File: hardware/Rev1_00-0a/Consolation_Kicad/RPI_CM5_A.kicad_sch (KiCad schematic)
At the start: 49 parts, among them J19 RPI_CMx_A, J7 2998TR, Q12 2N7002, U19 SN74LVC1G125DBVR, U21 MCP7940NT-I/MS, Y2 32.768kHz

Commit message: Update block diagram Updage charger schematic page with BQ25640 preliminary implementation
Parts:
- removed R111, R124: 4K7, footprint:RES_0402, symbol KicadCompDb:Resistors/RES_SMT_00010
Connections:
- net I2C6.I2C_SCL: no longer names the net of J19.47 (GPIO23)
- net I2C6.I2C_SDA: no longer names the net of J19.46 (GPIO22)

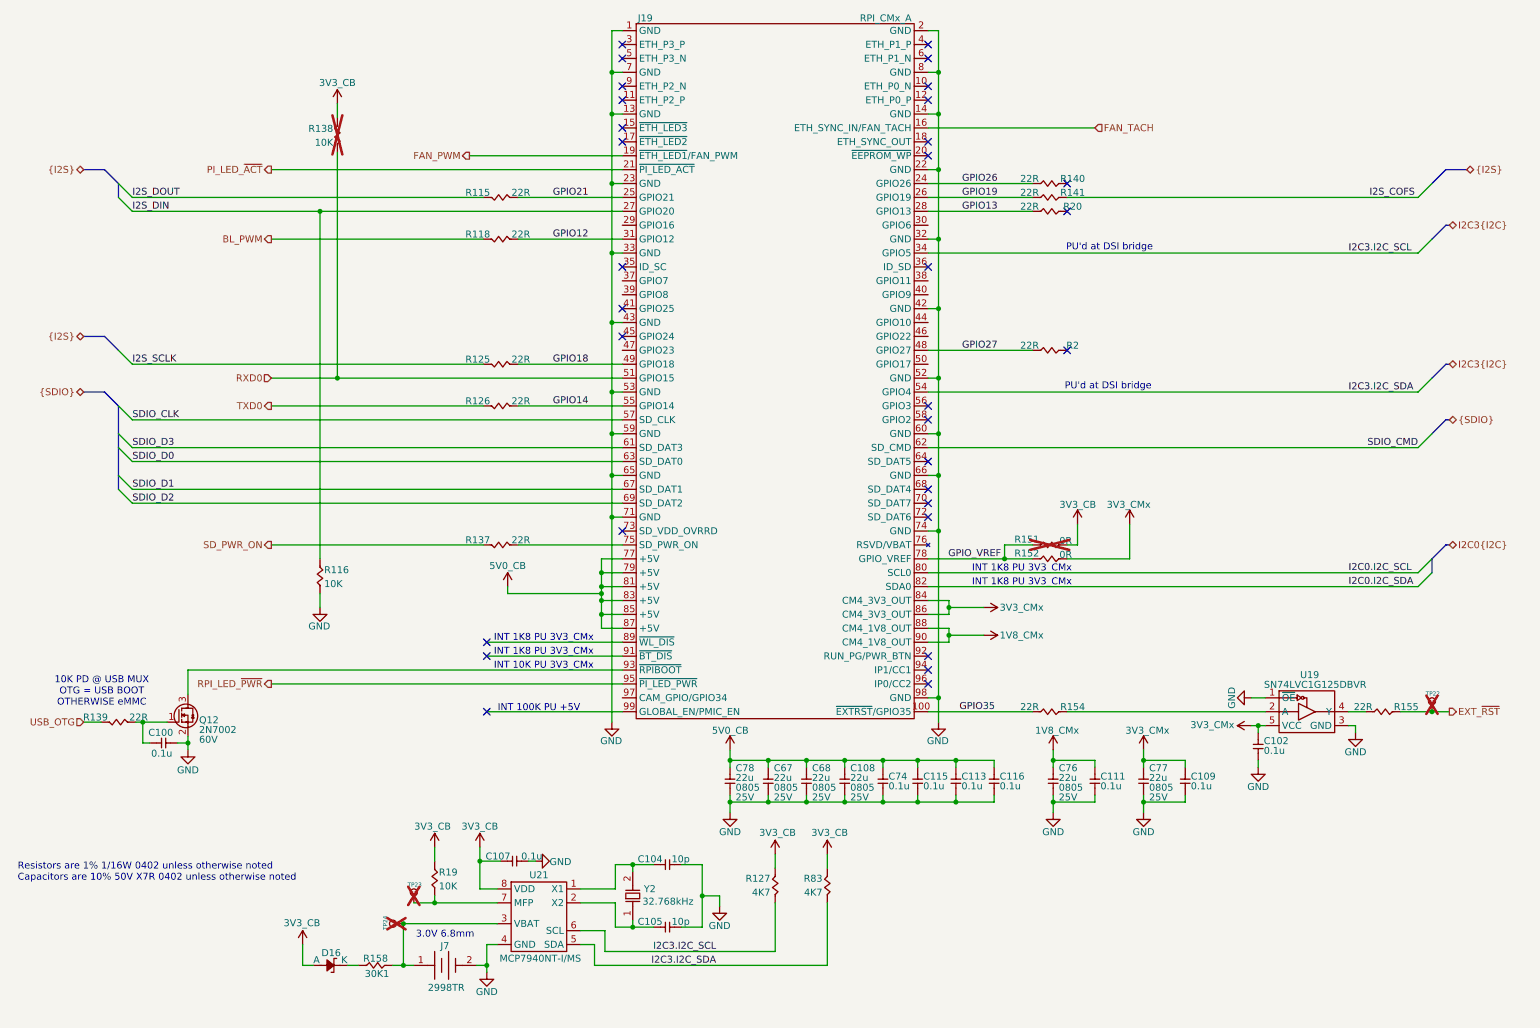
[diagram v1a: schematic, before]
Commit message: Add part number of codec to block diagram Add codec and hdmi schematic sheets
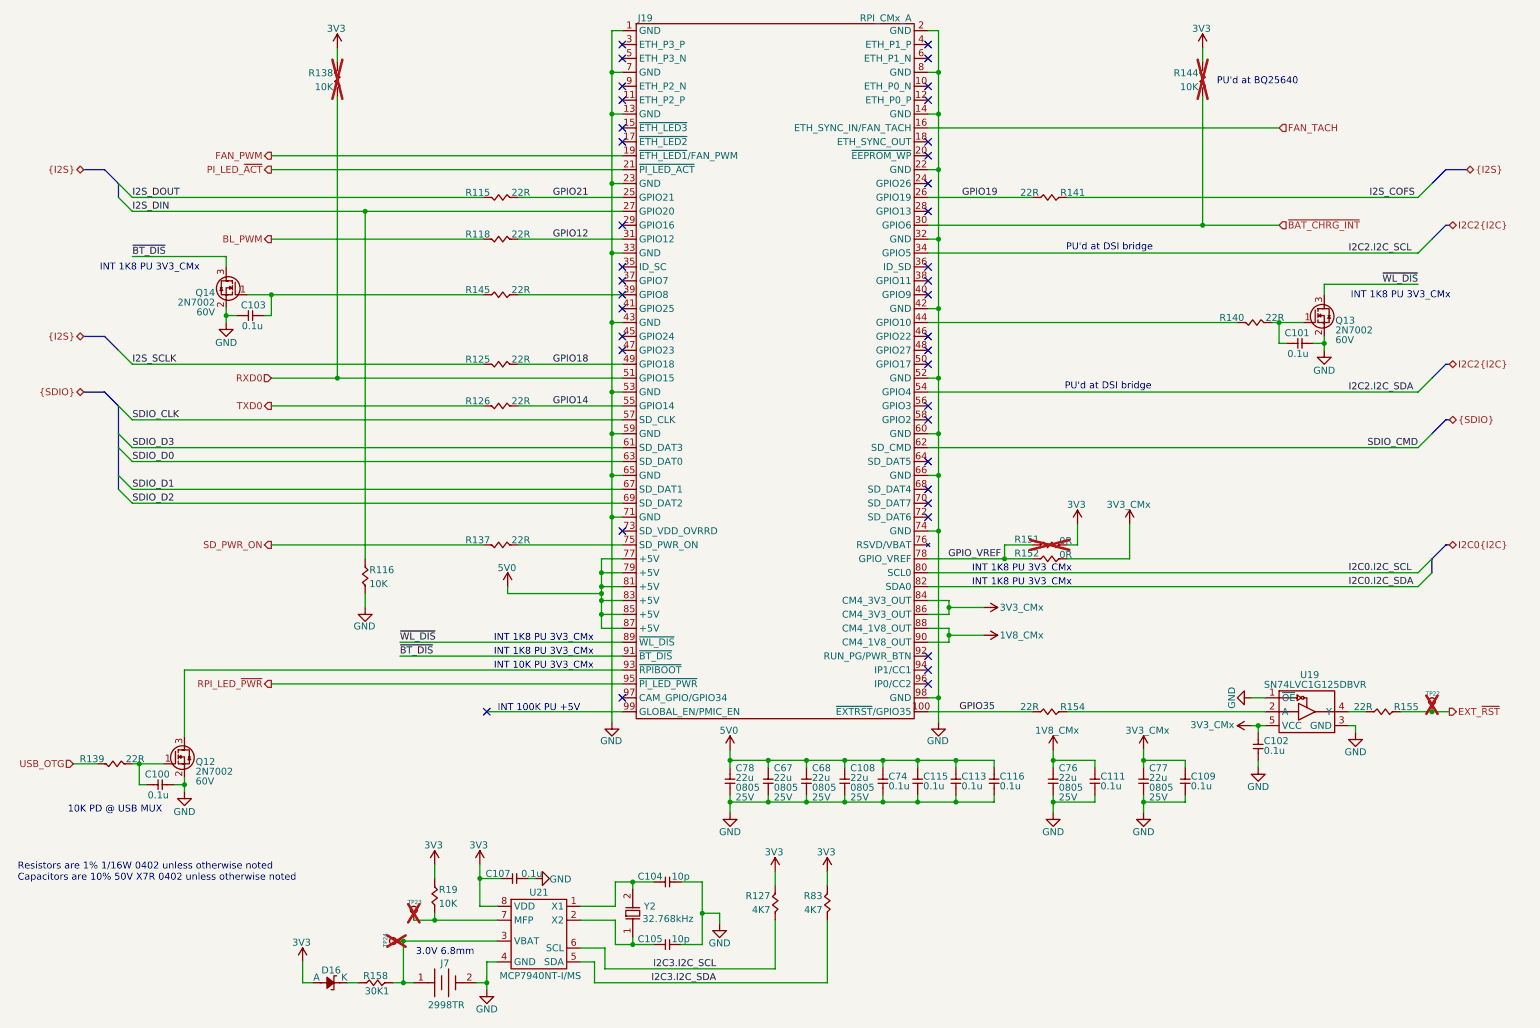
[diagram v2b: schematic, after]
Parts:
- removed R2, R20: 22R, footprint:RES_0402, symbol KicadCompDb:Resistors/RES_SMT_00015
- added C101, C103: 0.1u, footprint:CAP_NONPOL_0402, symbol KicadCompDb:Capacitors/CAP_CER_SMT_00001
- added Q13, Q14: 2N7002, footprint:SOT-23-3, symbol KicadCompDb:Mosfet/MOSFET_00001
- added R144: 10K, footprint:RES_0402, symbol KicadCompDb:Resistors/RES_SMT_00013
- added R145: 22R, footprint:RES_0402, symbol KicadCompDb:Resistors/RES_SMT_00015
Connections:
- net GND: now also C101.1, C103.1, Q13.2 (S), Q14.2 (S)
- net I2C3.I2C_SCL: no longer J19.34 (GPIO5)
- net I2C3.I2C_SDA: no longer J19.54 (GPIO4)
- net ~{BAT_CHRG_INT}: now reaches J19.30 (GPIO6)
- net ~{BAT_CHRG_INT}: now also R144.1
- net at J19.39 (GPIO8): now also R145.2
- net at J19.44 (GPIO10): now also R140.2
- net ~{WL_DIS}: now reaches J19.89 (~{WL_DIS})
- net ~{WL_DIS}: now also Q13.3 (D)
- net ~{BT_DIS}: now reaches J19.91 (~{BT_DIS})
- net ~{BT_DIS}: now also Q14.3 (D)
- net 3V3_CB renamed 3V3
- net 3V3: now also R144.2
- net 5V0_CB renamed 5V0
- net GPIO13: no longer names the net of J19.28 (GPIO13)
- net GPIO26: no longer names the net of R140.1
- net GPIO26: now also C101.2, Q13.1 (G); no longer J19.24 (GPIO26)
- net GPIO27: no longer names the net of J19.48 (GPIO27)
- new net: C103.2, Q14.1 (G), R145.1
- new net I2C2.I2C_SCL: J19.34 (GPIO5)
- new net I2C2.I2C_SDA: J19.54 (GPIO4)
- no-connect marks 32 -> 39
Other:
- note added: "10K PD @ USB MUX"
- note added: "PU'd at BQ25640"
- note removed: "10K PD @ USB MUX OTG = USB BOOT OTHERWISE eMMC"
- moved on the sheet: C100, C104, C105, C107, D16, J7, Q12, R116, R127, R138, R139, R158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

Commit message: Update schematics, block diagram and pin mux (good progress G)
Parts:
- removed TP23, TP24: 28 mils, footprint:SMT_TP_28_MILS, symbol KicadCompDb:Test Point/TP_00001
- added R117: 22R, footprint:RES_0402, symbol KicadCompDb:Resistors/RES_SMT_00015
- added R143, R156: 10K, footprint:RES_0402, symbol KicadCompDb:Resistors/RES_SMT_00013
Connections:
- net 3V3: now also R143.2, R156.2
- net FAN_PWM: now also R117.2; no longer J19.19 (~{ETH_LED1}/FAN_PWM)
- net GPIO10: now reaches J19.44 (GPIO10), R140.2
- net ~{VOL_UP}: now reaches J19.28 (GPIO13)
- net ~{VOL_UP}: now also R156.1
- net ~{VOL_DOWN}: now reaches J19.29 (GPIO16)
- net ~{VOL_DOWN}: now also R143.1
- net GPIO8: now reaches J19.39 (GPIO8), R145.2
- net PPS_RTC: now reaches J19.40 (GPIO9)
- net PPS_RTC: now also R19.1, U21.7 (MFP)
- net ~{HP_DETECT}: now reaches J19.50 (GPIO17)
- net I2C0.I2C_SCL: no longer names the net of J19.80 (SCL0)
- net I2C0.I2C_SDA: no longer names the net of J19.82 (SDA0)
- new net: J19.19 (~{ETH_LED1}/FAN_PWM), R117.1
- no-connect marks 39 -> 35
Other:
- note added: "INT 10K PU +5V"
- moved on the sheet: C100, C108, C109, C111, C113, C115, C116, C67, C68, C74, C76, C77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

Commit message: Update PinMux & Schematics
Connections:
- net RXD0 renamed CM5_RXD0
- net TXD0 renamed CM5_TXD0
- net ~{HP_DETECT}: no longer names the net of J19.50 (GPIO17)
- no-connect marks 35 -> 36
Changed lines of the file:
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@@
 	)
 	(no_connect
+		(at 179.07 78.105)
+	)
+	(no_connect
 		(at 179.07 62.865)
 	)
@@
 	(wire
 		(pts
-			(xy 179.07 78.105) (xy 227.965 78.105)
-		)
-		(stroke
-			(width 0)
-			(type default)
-		)
-	)
-	(wire
-		(pts
 			(xy 120.015 184.785) (xy 115.57 184.785)
 		)
@@
 		)
 	)
-	(hierarchical_label "RXD0"
+	(hierarchical_label "CM5_RXD0"
 		(shape input)
 		(at 74.295 80.645 180)
@@
 		)
 	)
-	(hierarchical_label "~{HP_DETECT}"
-		(shape input)
-		(at 227.965 78.105 0)
-		(effects
-			(font
-				(size 1.27 1.27)
-			)
-			(justify left)
-		)
-	)
 	(hierarchical_label "~{VOL_DOWN}"
 		(shape input)
@@
 		)
 	)
-	(hierarchical_label "TXD0"
+	(hierarchical_label "CM5_TXD0"
 		(shape output)
 		(at 74.295 85.725 180)

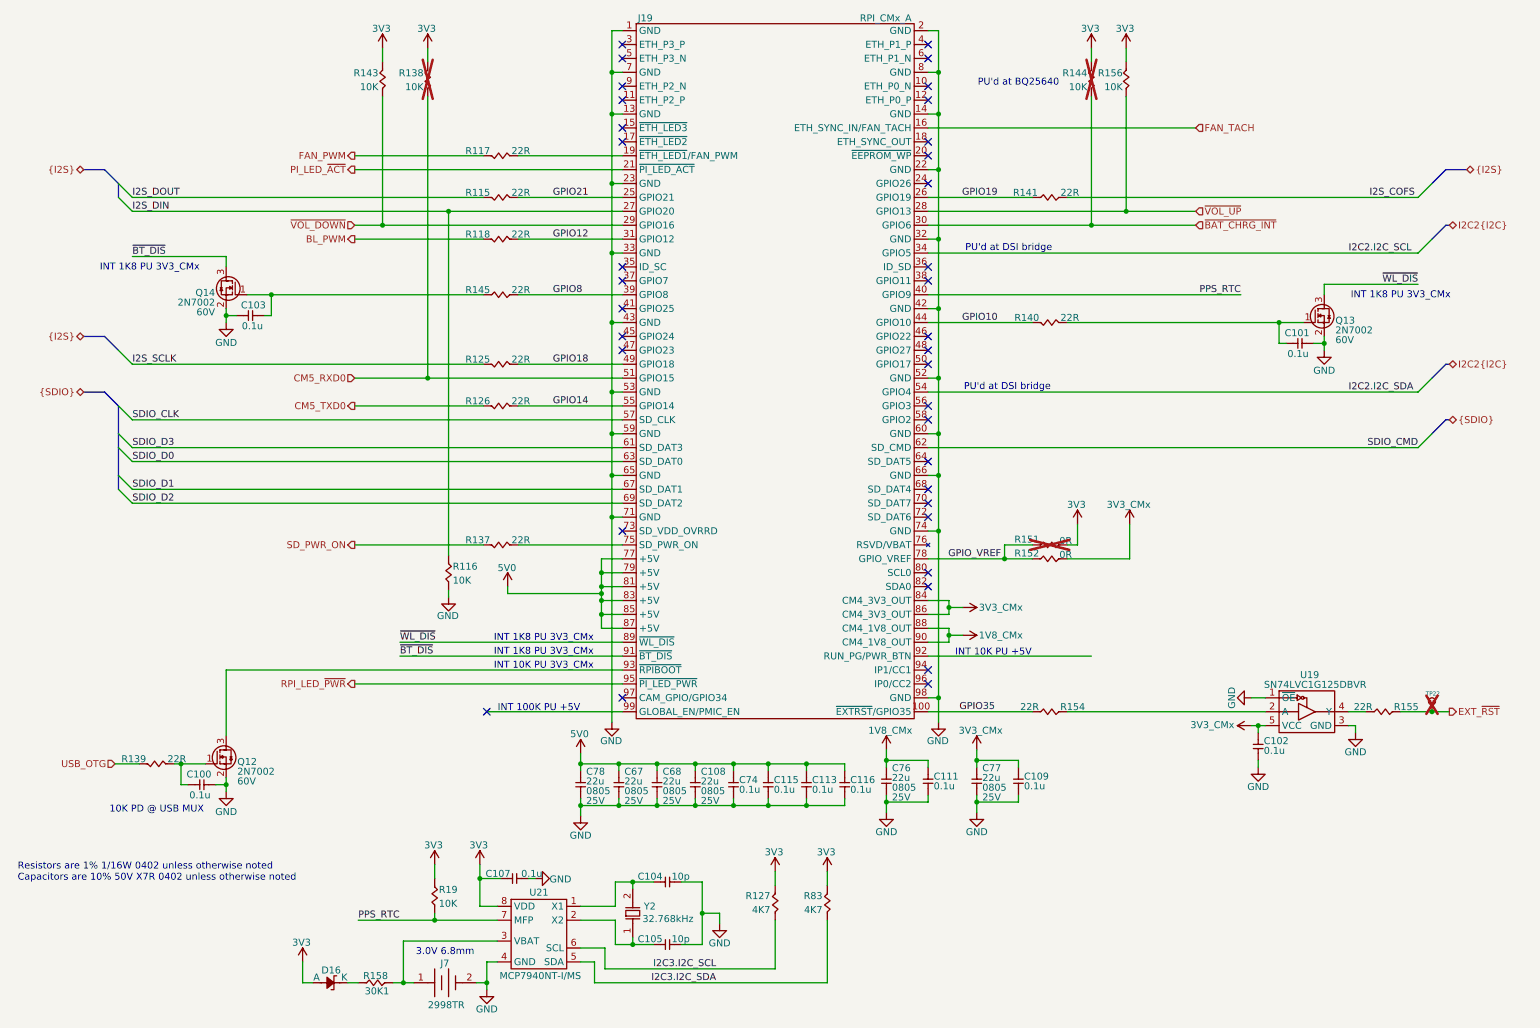
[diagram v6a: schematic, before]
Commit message: Work on block diagram and top-level schematic sheet Work on PinMux
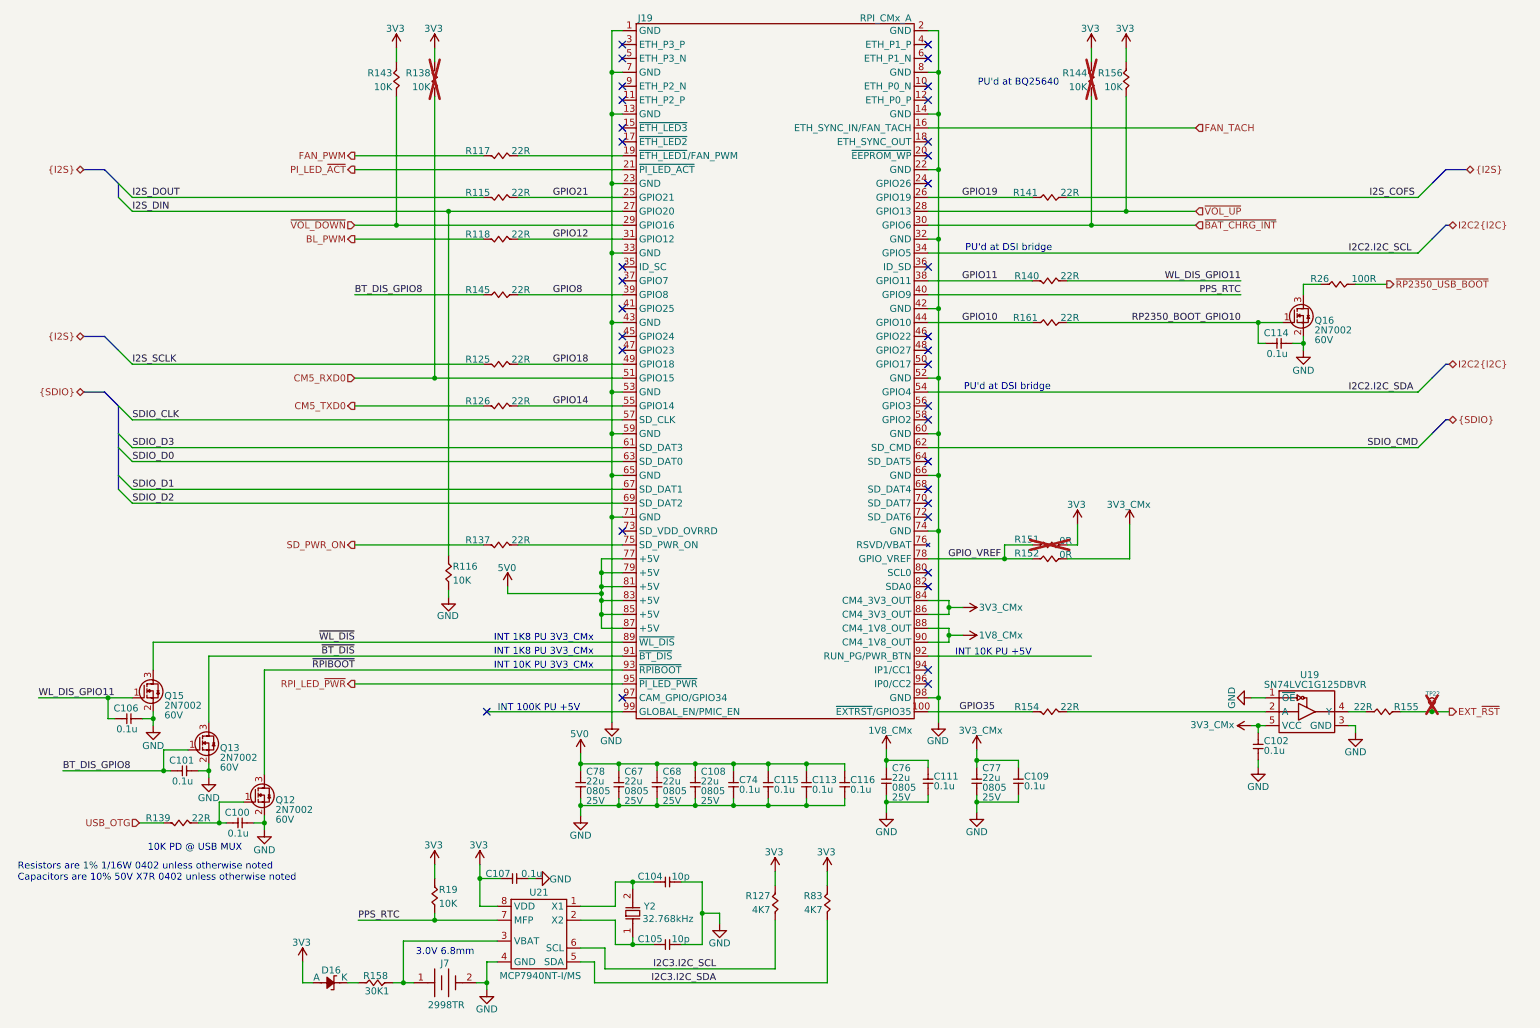
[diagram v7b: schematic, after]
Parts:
- removed C103: 0.1u, footprint:CAP_NONPOL_0402, symbol KicadCompDb:Capacitors/CAP_CER_SMT_00001
- removed Q14: 2N7002, footprint:SOT-23-3, symbol KicadCompDb:Mosfet/MOSFET_00001
- added C106, C114: 0.1u, footprint:CAP_NONPOL_0402, symbol KicadCompDb:Capacitors/CAP_CER_SMT_00001
- added Q15, Q16: 2N7002, footprint:SOT-23-3, symbol KicadCompDb:Mosfet/MOSFET_00001
- added R161: 22R, footprint:RES_0402, symbol KicadCompDb:Resistors/RES_SMT_00015
- added R26: 100R, footprint:RES_0402, symbol KicadCompDb:Resistors/RES_SMT_00035
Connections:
- net GND: now also C106.1, C114.1, Q15.2 (S), Q16.2 (S)
- net GPIO10: now also R161.1; no longer R140.2
- net GPIO35: now also R154.2; no longer R154.1
- net ~{BT_DIS}: now also Q13.3 (D)
- net ~{WL_DIS}: now also Q15.3 (D); no longer Q13.3 (D)
- net BT_DIS_GPIO8: now reaches C101.2, Q13.1 (G)
- net BT_DIS_GPIO8: now also R145.1; no longer R140.1
- net ~{RPIBOOT}: now reaches J19.93 (~{RPIBOOT}), Q12.3 (D)
- net GPIO11: now reaches J19.38 (GPIO11)
- net GPIO11: now also R140.2
- net at U19.2 (A): now also R154.1; no longer R154.2
- new net: Q16.3 (D), R26.2
- new net RP2350_BOOT_GPIO10: C114.2, Q16.1 (G), R161.2
- new net WL_DIS_GPIO11: C106.2, Q15.1 (G), R140.1
- new net ~{RP2350_USB_BOOT}: R26.1
- no-connect marks 36 -> 35
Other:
- moved on the sheet: C100, Q12, R138, R139, R143
